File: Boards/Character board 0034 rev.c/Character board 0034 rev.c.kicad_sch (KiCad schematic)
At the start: 43 parts, among them J1 card edge, J2 light connector, Q1 2N6125, U1 2.2K, U1 6821, U2 2.2K, U4 ULN2003A, U5 7406, U6 Board ID header

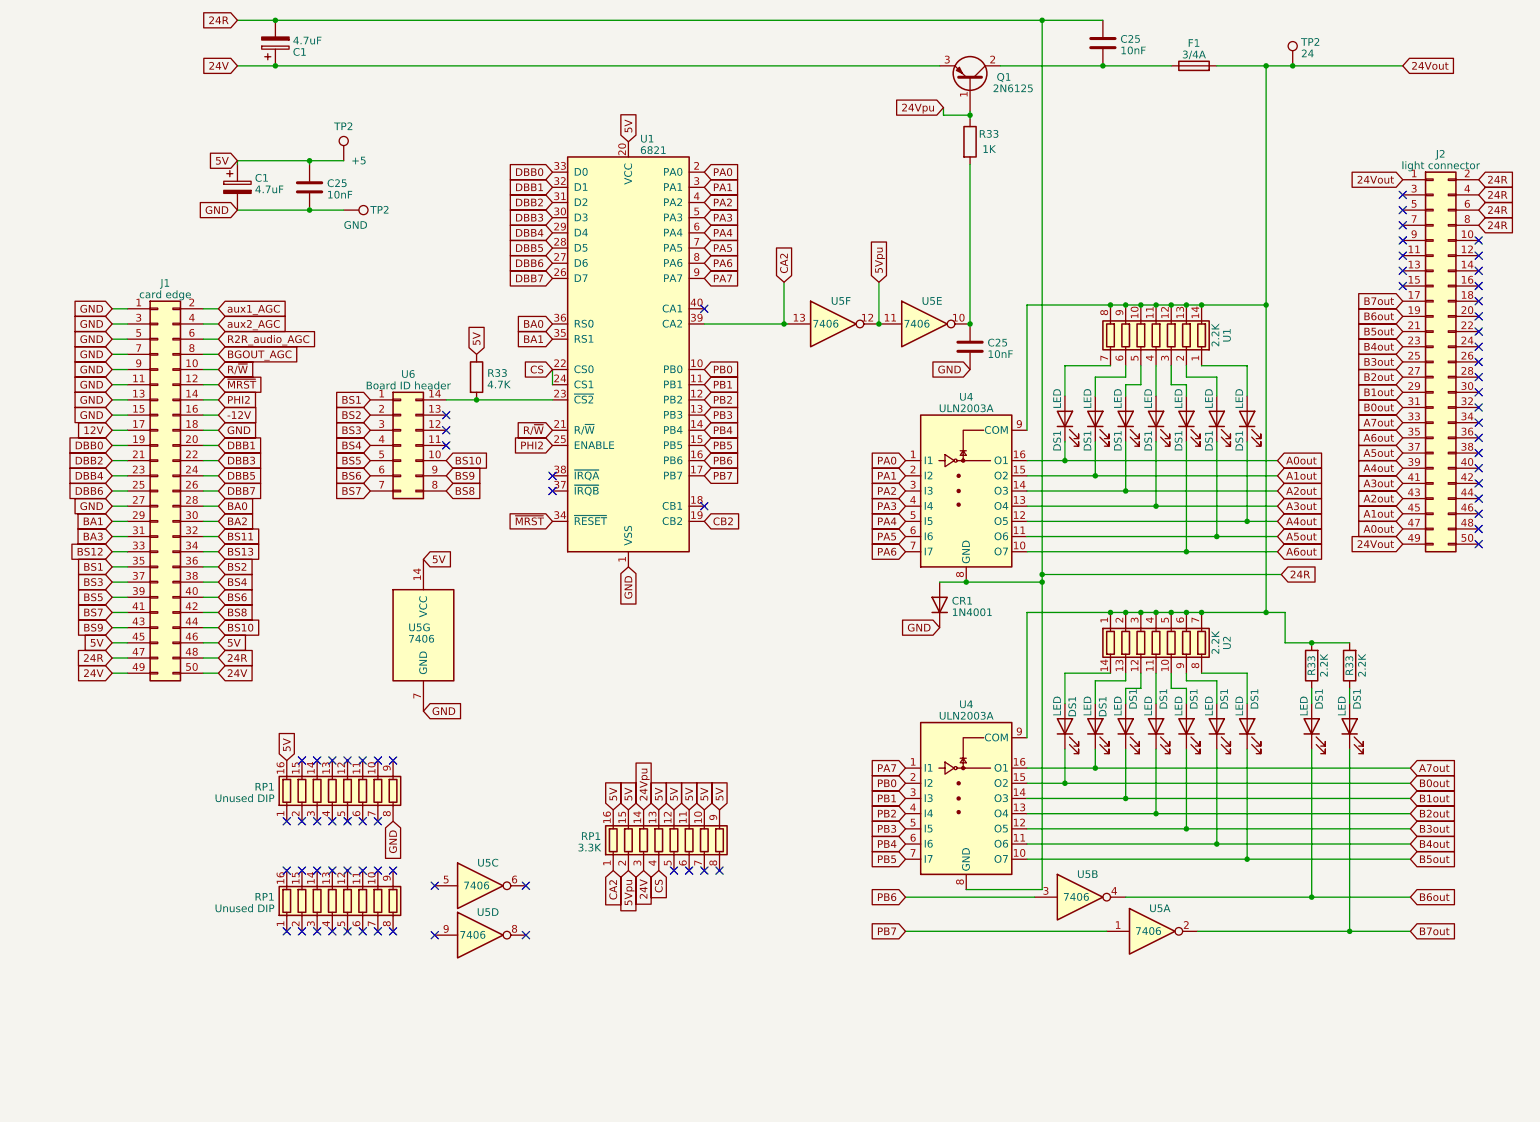
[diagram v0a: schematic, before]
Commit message: revised PCBs based on Jen's boards, added rev.c
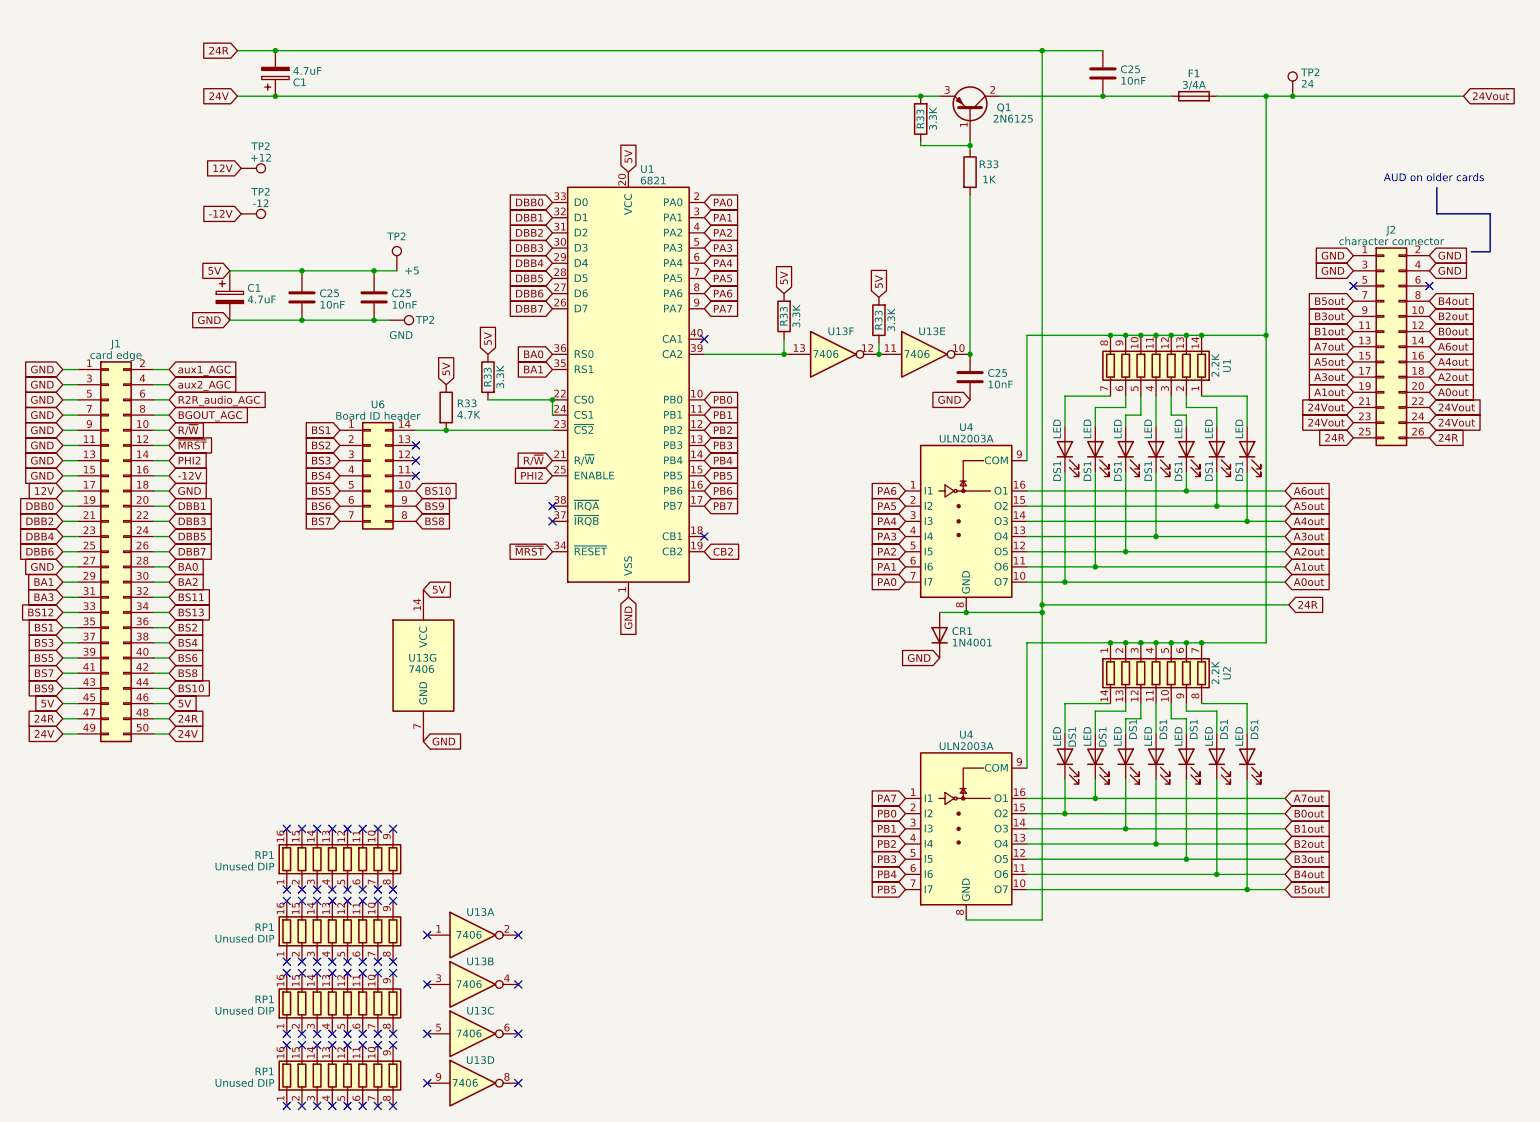
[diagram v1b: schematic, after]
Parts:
- removed DS1 (x2): LED, LED_THT:LED_D5.0mm_Horizontal_O3.81mm_Z15.0mm, symbol Device:LED
- removed J2: light connector, Connector_PinHeader_2.54mm:PinHeader_2x25_P2.54mm_Horizontal, symbol Connector_Generic:Conn_02x25_Odd_Even
- removed R33 (x2): 2.2K, Resistor_THT:R_Axial_DIN0309_L9.0mm_D3.2mm_P12.70mm_Horizontal, symbol Device:R
- removed RP1: 3.3K, Package_DIP:DIP-16_W7.62mm, symbol Device:R_Pack08
- added C25: 10nF, Capacitor_THT:C_Rect_L7.0mm_W2.5mm_P5.00mm, symbol Device:C
- added J2: character connector, Connector_PinHeader_2.54mm:PinHeader_2x13_P2.54mm_Horizontal, symbol Connector_Generic:Conn_02x13_Odd_Even
- added R33 (x4): 3.3K, Resistor_THT:R_Axial_DIN0309_L9.0mm_D3.2mm_P12.70mm_Horizontal, symbol Device:R
- added RP1 (x2): Unused DIP, Package_DIP:DIP-16_W7.62mm, symbol Device:R_Pack08
- added TP2: +12, TestPoint:TestPoint_Plated_Hole_D3.0mm, symbol Connector:TestPoint
- added TP2: -12, TestPoint:TestPoint_Plated_Hole_D3.0mm, symbol Connector:TestPoint
- renumbered U5 to U13
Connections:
- net -12V: now also TP2.1
- net 12V: now also TP2.1
- net 24R: now also J2.25 (Pin_25), J2.26 (Pin_26)
- net 24V: now also R33.2
- net 24Vout: now also J2.21 (Pin_21), J2.22 (Pin_22), J2.23 (Pin_23), J2.24 (Pin_24)
- net 5V: now also C25.1, R33.1, R33.2, R33.2; no longer RP1.16 (R1.2)
- net A0out: now also U4.10 (O7), J2.20 (Pin_20); no longer U4.16 (O1)
- net A1out: now also U4.11 (O6), J2.19 (Pin_19); no longer U4.15 (O2)
- net A2out: now also U4.12 (O5), J2.18 (Pin_18); no longer U4.14 (O3)
- net A3out: now also J2.17 (Pin_17)
- net A4out: now also U4.14 (O3), J2.16 (Pin_16); no longer U4.12 (O5)
- net A5out: now also U4.15 (O2), J2.15 (Pin_15); no longer U4.11 (O6)
- net A6out: now also U4.16 (O1), J2.14 (Pin_14); no longer U4.10 (O7)
- net A7out: now also J2.13 (Pin_13)
- net B0out: now also J2.12 (Pin_12)
- net B1out: now also J2.11 (Pin_11)
- net B2out: now also J2.10 (Pin_10)
- net B3out: now also J2.9 (Pin_9)
- net B4out: now also J2.8 (Pin_8)
- net B5out: now also J2.7 (Pin_7)
- net GND: now also C25.2, J2.1 (Pin_1), J2.2 (Pin_2), J2.3 (Pin_3), J2.4 (Pin_4); no longer RP1.8 (R8.1)
- net PA0: now also U4.7 (I7); no longer U4.1 (I1)
- net PA1: now also U4.6 (I6); no longer U4.2 (I2)
- net PA2: now also U4.5 (I5); no longer U4.3 (I3)
- net PA4: now also U4.3 (I3); no longer U4.5 (I5)
- net PA5: now also U4.2 (I2); no longer U4.6 (I6)
- net PA6: now also U4.1 (I1); no longer U4.7 (I7)
- net PB6: no longer U13.3
- net PB7: no longer U13.1
- net 24Vpu: no longer names the net of Q1.1 (B), R33.1
- net 24Vpu: now also R33.1
- net 5Vpu: no longer names the net of U13.11, U13.12
- net 5Vpu: now also R33.1
- net B6out: no longer names the net of U13.4
- net B7out: no longer names the net of U13.2
- net CA2: no longer names the net of U1.39 (CA2), U13.13
- net CA2: now also R33.1
- net CS: no longer names the net of U1.22 (CS0), U1.24 (CS1)
- net CS: now also R33.2
- no-connect marks 73 -> 81
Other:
- note added: "AUD on older cards"
- moved on the sheet: C1, C25, CR1, DS1, F1, J1, Q1, R33, RP1, TP2, U1, U13A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
